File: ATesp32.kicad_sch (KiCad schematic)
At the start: 22 parts, among them SW1 RESET, SW2 BOOT, U1 ESP32-S3, U2 ATmega32A-P, Y1 40 MHz

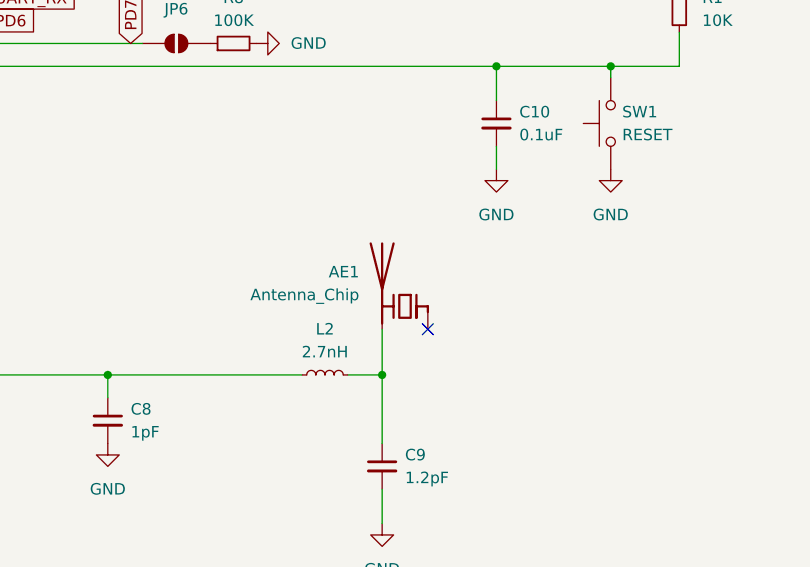
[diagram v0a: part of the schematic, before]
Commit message: antenna was backwards
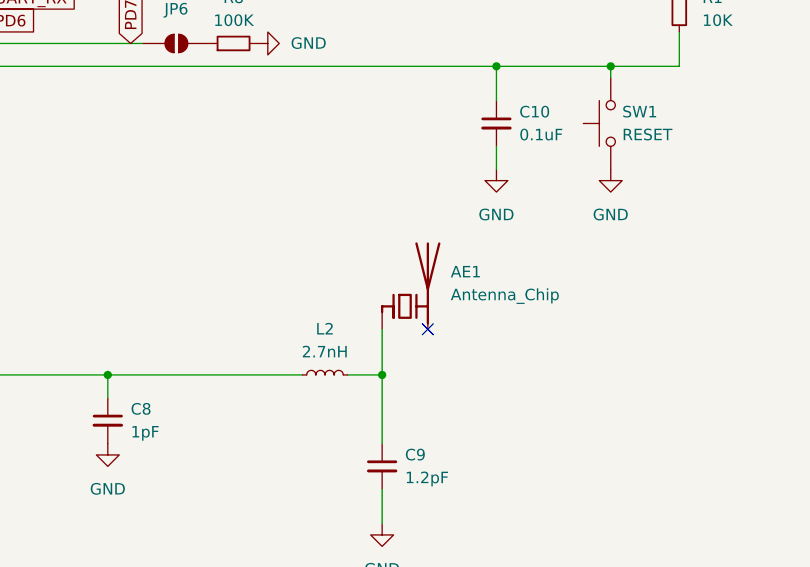
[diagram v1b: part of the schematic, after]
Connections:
- net at AE1.1 (FEED): now also C9.1, L2.2
- now unconnected: AE1.2 (PCB_Trace)
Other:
- moved on the sheet: AE1
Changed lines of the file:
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@@
 		(lib_id "Device:Antenna_Chip")
 		(at 168.91 154.94 0)
-		(mirror y)
 		(unit 1)
 		(exclude_from_sim no)
@@
 		(dnp no)
 		(property "Reference" "AE1"
-			(at 163.83 151.1299 0)
+			(at 173.99 151.1299 0)
 			(effects
 				(font
@@
 		)
 		(property "Value" "Antenna_Chip"
-			(at 163.83 153.6699 0)
+			(at 173.99 153.6699 0)
 			(effects
 				(font
@@
 		)
 		(property "Footprint" "RF_Antenna:Johanson_2450AT18x100"
-			(at 171.45 150.495 0)
+			(at 166.37 150.495 0)
 			(effects
 				(font
@@
 		)
 		(property "Datasheet" "~"
-			(at 171.45 150.495 0)
+			(at 166.37 150.495 0)
 			(effects
 				(font

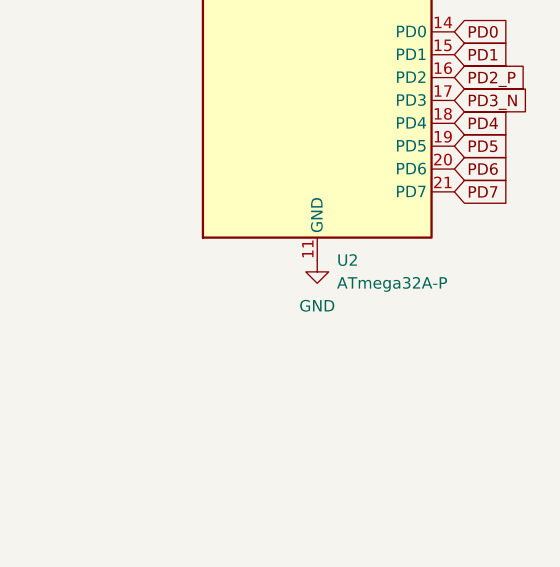
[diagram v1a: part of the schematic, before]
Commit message: spec components for JLC
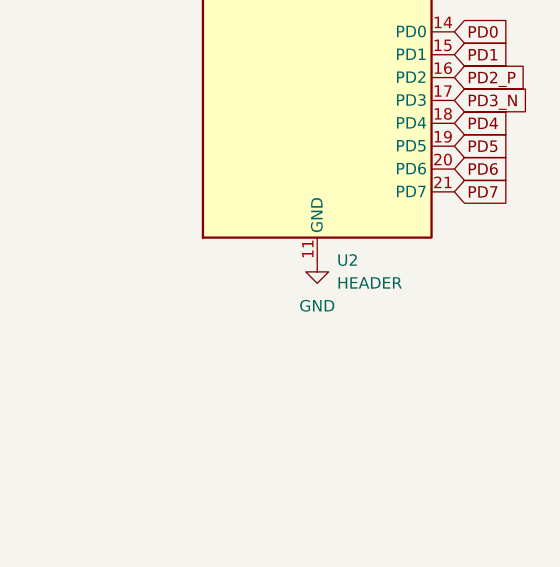
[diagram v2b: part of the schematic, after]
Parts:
- AE1: JLC (none) -> C89334
- C1, C10, C5, C6, C7: JLC (none) -> C1525
- C11, C12: JLC (none) -> C541434
- C3: JLC (none) -> C315248
- C8: DigiKey 13-AQ0603ARNPO9BN1R0CT-ND -> (none); JLC (none) -> C307340
- C9: DigiKey 13-AQ0603ARNPO9BN1R2CT-ND -> (none); JLC (none) -> C159808
- L2: DigiKey 495-B82496C3279Z000CT-ND -> (none); JLC (none) -> C434826
- R1: JLC (none) -> C25744
- R8: JLC (none) -> C25741
- R9: JLC (none) -> C4125
- SW1, SW2: JLC (none) -> C221680
- U1: JLC (none) -> C3013940; Mouser (none) -> 356-ESP32-S3FH4R2
- U2: value ATmega32A-P -> HEADER
- Y1: JLC (none) -> C255943; Mouser (none) -> 815-8W40-4B1UT

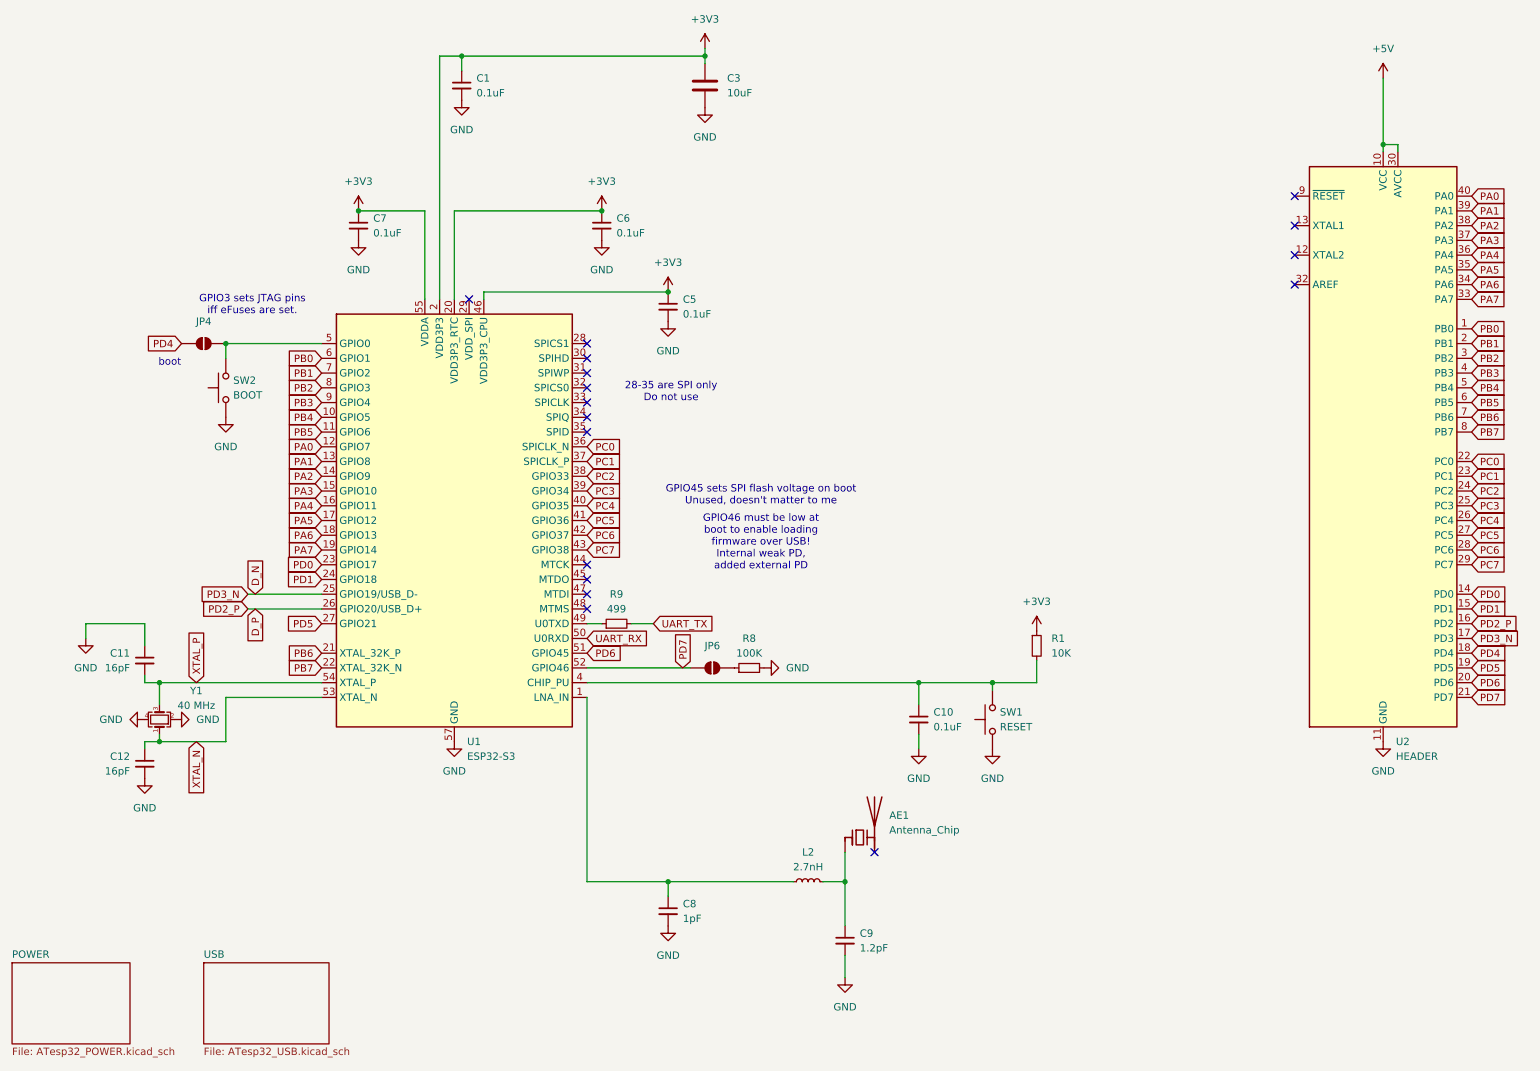
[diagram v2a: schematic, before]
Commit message: Generate production files. More clear part names for ESP and LiPo charger
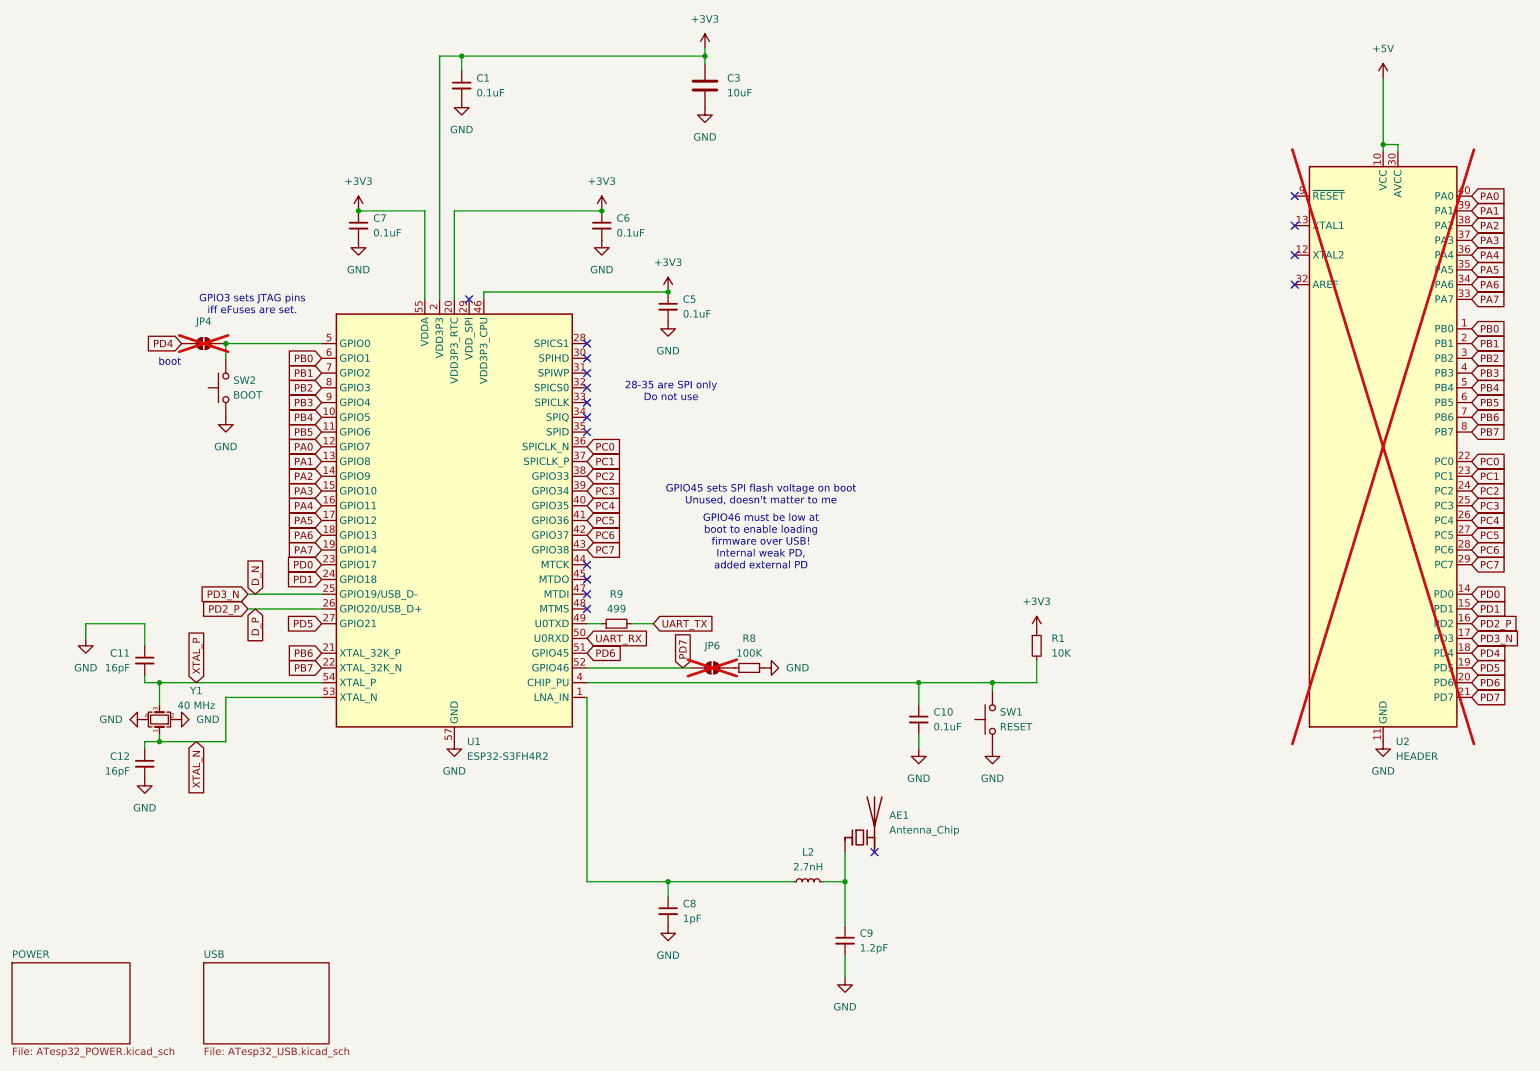
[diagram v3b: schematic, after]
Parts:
- JP4, JP6: now not fitted
- U1: value ESP32-S3 -> ESP32-S3FH4R2
- U2: now not fitted; now left out of the parts list
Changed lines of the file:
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@@
 		(unit 1)
 		(exclude_from_sim no)
-		(in_bom yes)
+		(in_bom no)
 		(on_board yes)
-		(dnp no)
+		(dnp yes)
 		(fields_autoplaced yes)
 		(property "Reference" "U2"
@@
 		(in_bom no)
 		(on_board yes)
-		(dnp no)
+		(dnp yes)
 		(fields_autoplaced yes)
 		(property "Reference" "JP6"
@@
 			)
 		)
-		(property "Value" "ESP32-S3"
+		(property "Value" "ESP32-S3FH4R2"
 			(at 101.2541 140.97 0)
 			(effects
@@
 		(in_bom no)
 		(on_board yes)
-		(dnp no)
+		(dnp yes)
 		(fields_autoplaced yes)
 		(property "Reference" "JP4"

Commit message: generated manf files. Too damn expensive, adjusting min track and holes
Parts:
- AE1: JLC C89334 -> (none); LCSC (none) -> C89334
- C1, C10, C5, C6, C7: JLC C1525 -> (none); LCSC (none) -> C1525
- C11, C12: JLC C541434 -> (none); LCSC (none) -> C541434
- C3: JLC C315248 -> (none); LCSC (none) -> C315248
- C8: JLC C307340 -> (none); LCSC (none) -> C307340
- C9: JLC C159808 -> (none); LCSC (none) -> C159808
- L2: JLC C434826 -> (none); LCSC (none) -> C434826
- R1: JLC C25744 -> (none); LCSC (none) -> C25744
- R8: JLC C25741 -> (none); LCSC (none) -> C25741
- R9: JLC C4125 -> (none); LCSC (none) -> C4125
- SW1, SW2: JLC C221680 -> (none); LCSC (none) -> C221680
- U1: JLC C3013940 -> (none); LCSC (none) -> C3013940
- Y1: JLC C255943 -> (none); LCSC (none) -> C255943
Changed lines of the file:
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@@
 			)
 		)
-		(property "JLC" "C1525"
+		(property "Sim.Device" ""
 			(at 135.89 63.5 0)
 			(effects
@@
 			)
 		)
-		(property "Sim.Device" ""
+		(property "Sim.Pins" ""
 			(at 135.89 63.5 0)
 			(effects
@@
 			)
 		)
-		(property "Sim.Pins" ""
+		(property "Sim.Type" ""
 			(at 135.89 63.5 0)
 			(effects
@@
 			)
 		)
-		(property "Sim.Type" ""
+		(property "LCSC" "C1525"
 			(at 135.89 63.5 0)
 			(effects
@@
 			)
 		)
-		(property "JLC" "C89334"
+		(property "Sim.Device" ""
 			(at 168.91 154.94 0)
 			(effects
@@
 			)
 		)
-		(property "Sim.Device" ""
+		(property "Sim.Pins" ""
 			(at 168.91 154.94 0)
 			(effects
@@
 			)
 		)
-		(property "Sim.Pins" ""
+		(property "Sim.Type" ""
 			(at 168.91 154.94 0)
 			(effects
@@
 			)
 		)
-		(property "Sim.Type" ""
+		(property "LCSC" "C89334"
 			(at 168.91 154.94 0)
 			(effects
@@
 			)
 		)
-		(property "JLC" "C255943"
+		(property "LCSC" "C255943"
 			(at 48.26 134.62 0)
 			(effects
@@
 			)
 		)
-		(property "JLC" "C541434"
+		(property "Sim.Device" ""
 			(at 45.72 124.46 0)
 			(effects
@@
 			)
 		)
-		(property "Sim.Device" ""
+		(property "Sim.Pins" ""
 			(at 45.72 124.46 0)
 			(effects
@@
 			)
 		)
-		(property "Sim.Pins" ""
+		(property "Sim.Type" ""
 			(at 45.72 124.46 0)
 			(effects
@@
 			)
 		)
-		(property "Sim.Type" ""
+		(property "LCSC" "C541434"
 			(at 45.72 124.46 0)
 			(effects
@@
 			)
 		)
-		(property "JLC" "C3013940"
+		(property "Mouser" "356-ESP32-S3FH4R2"
 			(at 99.06 100.33 0)
 			(effects
@@
 			)
 		)
-		(property "Mouser" "356-ESP32-S3FH4R2"
+		(property "Sim.Device" ""
 			(at 99.06 100.33 0)
 			(effects
@@
 			)
 		)
-		(property "Sim.Device" ""
+		(property "Sim.Pins" ""
 			(at 99.06 100.33 0)
 			(effects
@@
 			)
 		)
-		(property "Sim.Pins" ""
+		(property "Sim.Type" ""
 			(at 99.06 100.33 0)
 			(effects
@@
 			)
 		)
-		(property "Sim.Type" ""
+		(property "LCSC" "C3013940"
 			(at 99.06 100.33 0)
 			(effects
@@
 			)
 		)
-		(property "JLC" "C159808"
+		(property "Sim.Device" ""
 			(at 166.37 172.72 0)
 			(effects
@@
 			)
 		)
-		(property "Sim.Device" ""
+		(property "Sim.Pins" ""
 			(at 166.37 172.72 0)
 			(effects
@@
 			)
 		)
-		(property "Sim.Pins" ""
+		(property "Sim.Type" ""
 			(at 166.37 172.72 0)
 			(effects
@@
 			)
 		)
-		(property "Sim.Type" ""
+		(property "LCSC" "C159808"
 			(at 166.37 172.72 0)
 			(effects
@@
 			)
 		)
-		(property "JLC" "C315248"
+		(property "Sim.Device" ""
 			(at 142.24 25.4 0)
 			(effects
@@
 			)
 		)
-		(property "Sim.Device" ""
+		(property "Sim.Pins" ""
 			(at 142.24 25.4 0)
 			(effects
@@
 			)
 		)
-		(property "Sim.Pins" ""
+		(property "Sim.Type" ""
 			(at 142.24 25.4 0)
 			(effects
@@
 			)
 		)
-		(property "Sim.Type" ""
+		(property "LCSC" "C315248"
 			(at 142.24 25.4 0)
 			(effects
@@
 			)
 		)
-		(property "JLC" "C1525"
+		(property "Sim.Device" ""
 			(at 124.46 49.53 0)
 			(effects
@@
 			)
 		)
-		(property "Sim.Device" ""
+		(property "Sim.Pins" ""
 			(at 124.46 49.53 0)
 			(effects
@@
 			)
 		)
-		(property "Sim.Pins" ""
+		(property "Sim.Type" ""
 			(at 124.46 49.53 0)
 			(effects
@@
 			)
 		)
-		(property "Sim.Type" ""
+		(property "LCSC" "C1525"
 			(at 124.46 49.53 0)
 			(effects
@@
 			)
 		)
-		(property "JLC" "C1525"
+		(property "Sim.Device" ""
 			(at 100.33 25.4 0)
 			(effects
@@
 			)
 		)
-		(property "Sim.Device" ""
+		(property "Sim.Pins" ""
 			(at 100.33 25.4 0)
 			(effects
@@
 			)
 		)
-		(property "Sim.Pins" ""
+		(property "Sim.Type" ""
 			(at 100.33 25.4 0)
 			(effects
@@
 			)
 		)
-		(property "Sim.Type" ""
+		(property "LCSC" "C1525"
 			(at 100.33 25.4 0)
 			(effects
@@
 			)
 		)
-		(property "JLC" "C221680"
+		(property "LCSC" "C221680"
 			(at 191.77 134.62 0)
 			(effects
@@
 			)
 		)
-		(property "JLC" "C1525"
+		(property "Sim.Device" ""
 			(at 82.55 49.53 0)
 			(effects
@@
 			)
 		)
-		(property "Sim.Device" ""
+		(property "Sim.Pins" ""
 			(at 82.55 49.53 0)
 			(effects
@@
 			)
 		)
-		(property "Sim.Pins" ""
+		(property "Sim.Type" ""
 			(at 82.55 49.53 0)
 			(effects
@@
 			)
 		)
-		(property "Sim.Type" ""
+		(property "LCSC" "C1525"
 			(at 82.55 49.53 0)
 			(effects
@@
 			)
 		)
-		(property "JLC" "C307340"
+		(property "Sim.Device" ""
 			(at 135.89 167.64 0)
 			(effects
@@
 			)
 		)
-		(property "Sim.Device" ""
+		(property "Sim.Pins" ""
 			(at 135.89 167.64 0)
 			(effects
@@
 			)
 		)
-		(property "Sim.Pins" ""
+		(property "Sim.Type" ""
 			(at 135.89 167.64 0)
 			(effects
@@
 			)
 		)
-		(property "Sim.Type" ""
+		(property "LCSC" "C307340"
 			(at 135.89 167.64 0)
 			(effects
@@
 			)
 		)
-		(property "JLC" "C541434"
+		(property "Sim.Device" ""
 			(at 45.72 142.24 0)
 			(effects
@@
 			)
 		)
-		(property "Sim.Device" ""
+		(property "Sim.Pins" ""
 			(at 45.72 142.24 0)
 			(effects
@@
 			)
 		)
-		(property "Sim.Pins" ""
+		(property "Sim.Type" ""
 			(at 45.72 142.24 0)
 			(effects
@@
 			)
 		)
-		(property "Sim.Type" ""
+		(property "LCSC" "C541434"
 			(at 45.72 142.24 0)
 			(effects
@@
 			)
 		)
-		(property "JLC" "C25741"
+		(property "LCSC" "C25741"
 			(at 149.86 125.73 0)
 			(effects
@@
 			)
 		)
-		(property "JLC" "C4125"
+		(property "LCSC" "C4125"
 			(at 127 118.11 0)
 			(effects
@@
 			)
 		)
-		(property "JLC" "C25744"
+		(property "LCSC" "C25744"
 			(at 199.39 121.92 0)
 			(effects
@@
 			)
 		)
-		(property "JLC" "C221680"
+		(property "LCSC" "C221680"
 			(at 59.69 77.47 0)
 			(effects
@@
 			)
 		)
-		(property "JLC" "C1525"
+		(property "Sim.Device" ""
 			(at 179.07 134.62 0)
 			(effects
@@
 			)
 		)
-		(property "Sim.Device" ""
+		(property "Sim.Pins" ""
 			(at 179.07 134.62 0)
 			(effects
@@
 			)
 		)
-		(property "Sim.Pins" ""
+		(property "Sim.Type" ""
 			(at 179.07 134.62 0)
 			(effects
@@
 			)
 		)
-		(property "Sim.Type" ""
+		(property "LCSC" "C1525"
 			(at 179.07 134.62 0)
 			(effects
@@
 			)
 		)
-		(property "JLC" "C434826"
+		(property "LCSC" "C434826"
 			(at 160.02 162.56 0)
 			(effects

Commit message: Add some Mouser PNs
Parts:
- AE1: Mouser (none) -> 609-2450AT18B0100001
- C1, C10, C5, C6, C7: DigiKey (none) -> 1276-1001-1-ND; Mouser (none) -> 187-CL05B104KO5NNNC
- C11, C12: DigiKey (none) -> 13-CC0402FRNPO9BN160CT-ND
- C3: DigiKey (none) -> 1276-1450-1-ND
- C8: DigiKey (none) -> 1276-6609-1-ND
- C9: DigiKey (none) -> 1276-1654-1-ND
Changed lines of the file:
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@@
 			)
 		)
+		(property "DigiKey" "1276-1001-1-ND"
+			(at 135.89 63.5 0)
+			(effects
+				(font
+					(size 1.27 1.27)
+				)
+				(hide yes)
+			)
+		)
+		(property "Mouser" "187-CL05B104KO5NNNC"
+			(at 135.89 63.5 0)
+			(effects
+				(font
+					(size 1.27 1.27)
+				)
+				(hide yes)
+			)
+		)
 		(pin "1"
 		)
@@
 			)
 		)
+		(property "Mouser" " 609-2450AT18B0100001"
+			(at 168.91 154.94 0)
+			(effects
+				(font
+					(size 1.27 1.27)
+				)
+				(hide yes)
+			)
+		)
 		(pin "2"
 		)
@@
 			)
 		)
+		(property "DigiKey" "13-CC0402FRNPO9BN160CT-ND"
+			(at 45.72 124.46 0)
+			(effects
+				(font
+					(size 1.27 1.27)
+				)
+				(hide yes)
+			)
+		)
 		(pin "2"
 		)
@@
 			)
 		)
-		(property "DigiKey" ""
+		(property "DigiKey" "1276-1654-1-ND"
 			(at 166.37 172.72 0)
 			(effects
@@
 			)
 		)
+		(property "DigiKey" "1276-1450-1-ND"
+			(at 142.24 25.4 0)
+			(effects
+				(font
+					(size 1.27 1.27)
+				)
+				(hide yes)
+			)
+		)
 		(pin "1"
 		)
@@
 			)
 		)
+		(property "DigiKey" "1276-1001-1-ND"
+			(at 124.46 49.53 0)
+			(effects
+				(font
+					(size 1.27 1.27)
+				)
+				(hide yes)
+			)
+		)
+		(property "Mouser" "187-CL05B104KO5NNNC"
+			(at 124.46 49.53 0)
+			(effects
+				(font
+					(size 1.27 1.27)
+				)
+				(hide yes)
+			)
+		)
 		(pin "1"
 		)
@@
 			)
 		)
+		(property "DigiKey" "1276-1001-1-ND"
+			(at 100.33 25.4 0)
+			(effects
+				(font
+					(size 1.27 1.27)
+				)
+				(hide yes)
+			)
+		)
+		(property "Mouser" "187-CL05B104KO5NNNC"
+			(at 100.33 25.4 0)
+			(effects
+				(font
+					(size 1.27 1.27)
+				)
+				(hide yes)
+			)
+		)
 		(pin "1"
 		)
@@
 			)
 		)
+		(property "DigiKey" "1276-1001-1-ND"
+			(at 82.55 49.53 0)
+			(effects
+				(font
+					(size 1.27 1.27)
+				)
+				(hide yes)
+			)
+		)
+		(property "Mouser" "187-CL05B104KO5NNNC"
+			(at 82.55 49.53 0)
+			(effects
+				(font
+					(size 1.27 1.27)
+				)
+				(hide yes)
+			)
+		)
 		(pin "1"
 		)
@@
 			)
 		)
-		(property "DigiKey" ""
+		(property "DigiKey" "1276-6609-1-ND"
 			(at 135.89 167.64 0)
 			(effects
@@
 			)
 		)
+		(property "DigiKey" "13-CC0402FRNPO9BN160CT-ND"
+			(at 45.72 142.24 0)
+			(effects
+				(font
+					(size 1.27 1.27)
+				)
+				(hide yes)
+			)
+		)
 		(pin "1"
 		)
@@
 			(at 179.07 134.62 0)
 			(effects
+				(font
+					(size 1.27 1.27)
+				)
+				(hide yes)
+			)
+		)
+		(property "DigiKey" "1276-1001-1-ND"
+			(at 179.07 134.62 0)
+			(effects
+				(font
+					(size 1.27 1.27)
+				)
+				(hide yes)
+			)
+		)
+		(property "Mouser" "187-CL05B104KO5NNNC"
+			(at 179.07 134.62 0)
+			(effects

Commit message: update manf outputs
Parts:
- C1, C10, C5, C6, C7: Mouser 187-CL05B104KO5NNNC -> (none)
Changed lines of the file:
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@@
 			)
 		)
-		(property "Mouser" "187-CL05B104KO5NNNC"
+		(property "Mouser" ""
 			(at 135.89 63.5 0)
 			(effects
@@
 			)
 		)
-		(property "Mouser" "187-CL05B104KO5NNNC"
+		(property "Mouser" ""
 			(at 124.46 49.53 0)
 			(effects
@@
 			)
 		)
-		(property "Mouser" "187-CL05B104KO5NNNC"
+		(property "Mouser" ""
 			(at 100.33 25.4 0)
 			(effects
@@
 			)
 		)
-		(property "Mouser" "187-CL05B104KO5NNNC"
+		(property "Mouser" ""
 			(at 82.55 49.53 0)
 			(effects
@@
 			)
 		)
-		(property "Mouser" "187-CL05B104KO5NNNC"
+		(property "Mouser" ""
 			(at 179.07 134.62 0)
 			(effects
